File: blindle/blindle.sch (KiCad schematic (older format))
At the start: 8 parts, among them J1 CONN_5V, J2 CONN_8V, M1 74HC595, P1 pololua4988, P2 pololua4988

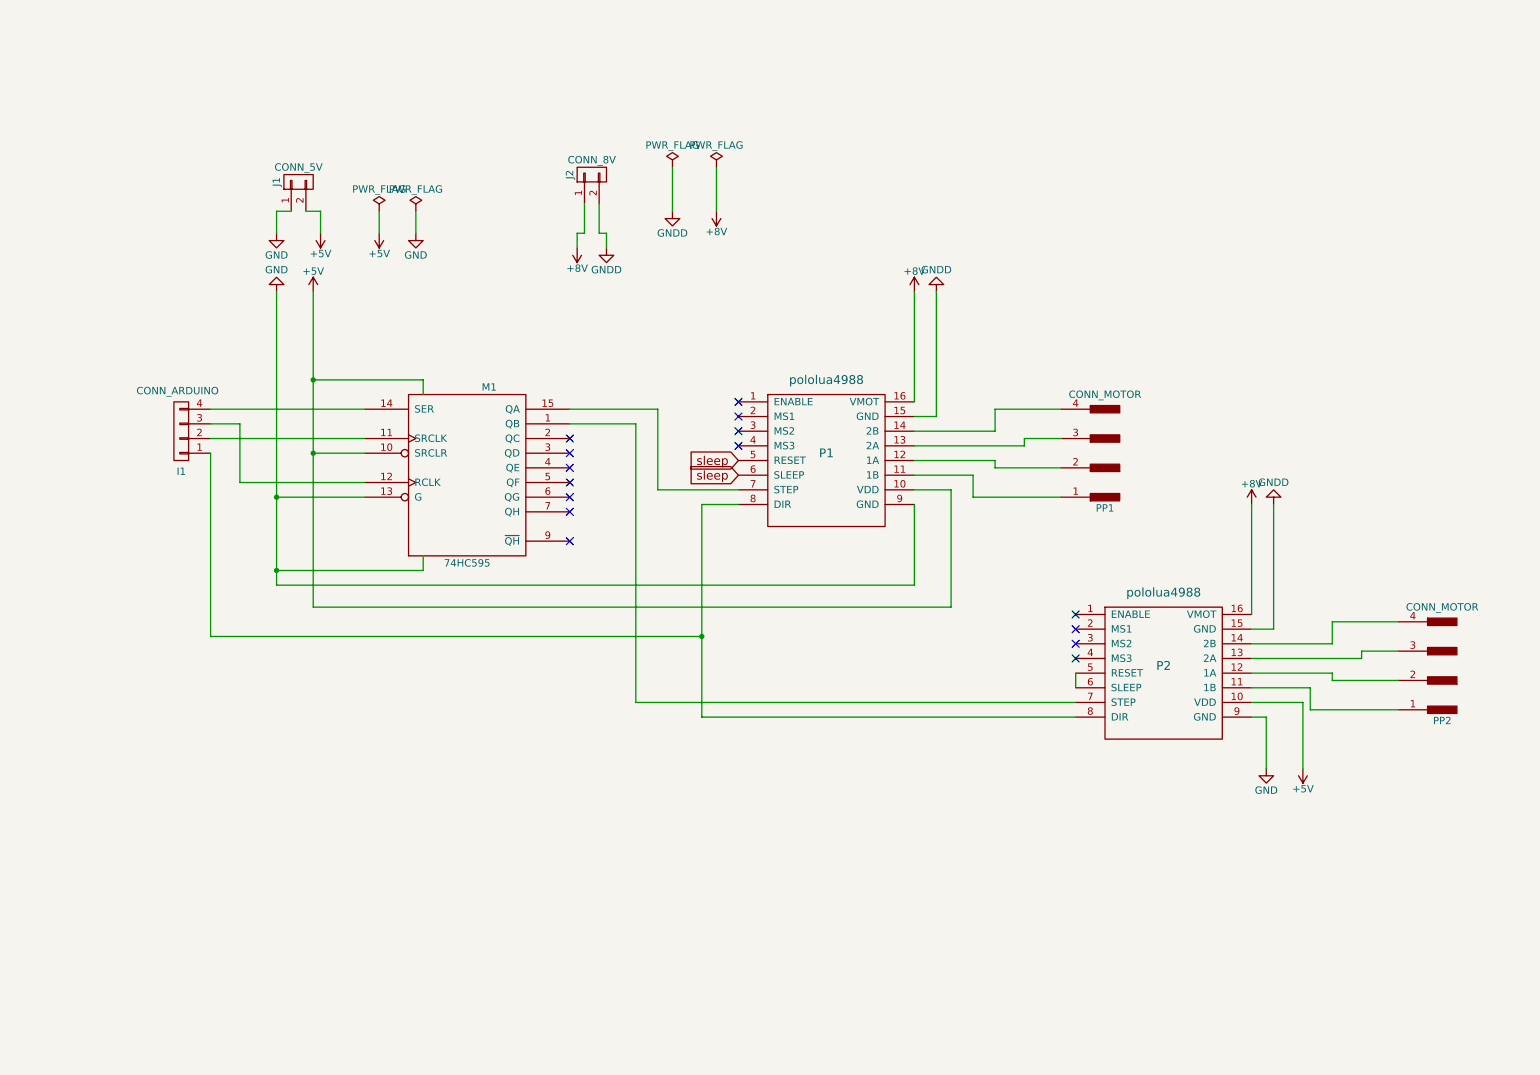
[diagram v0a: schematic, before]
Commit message: Bug en plantilla pololu - Version 4 pololus
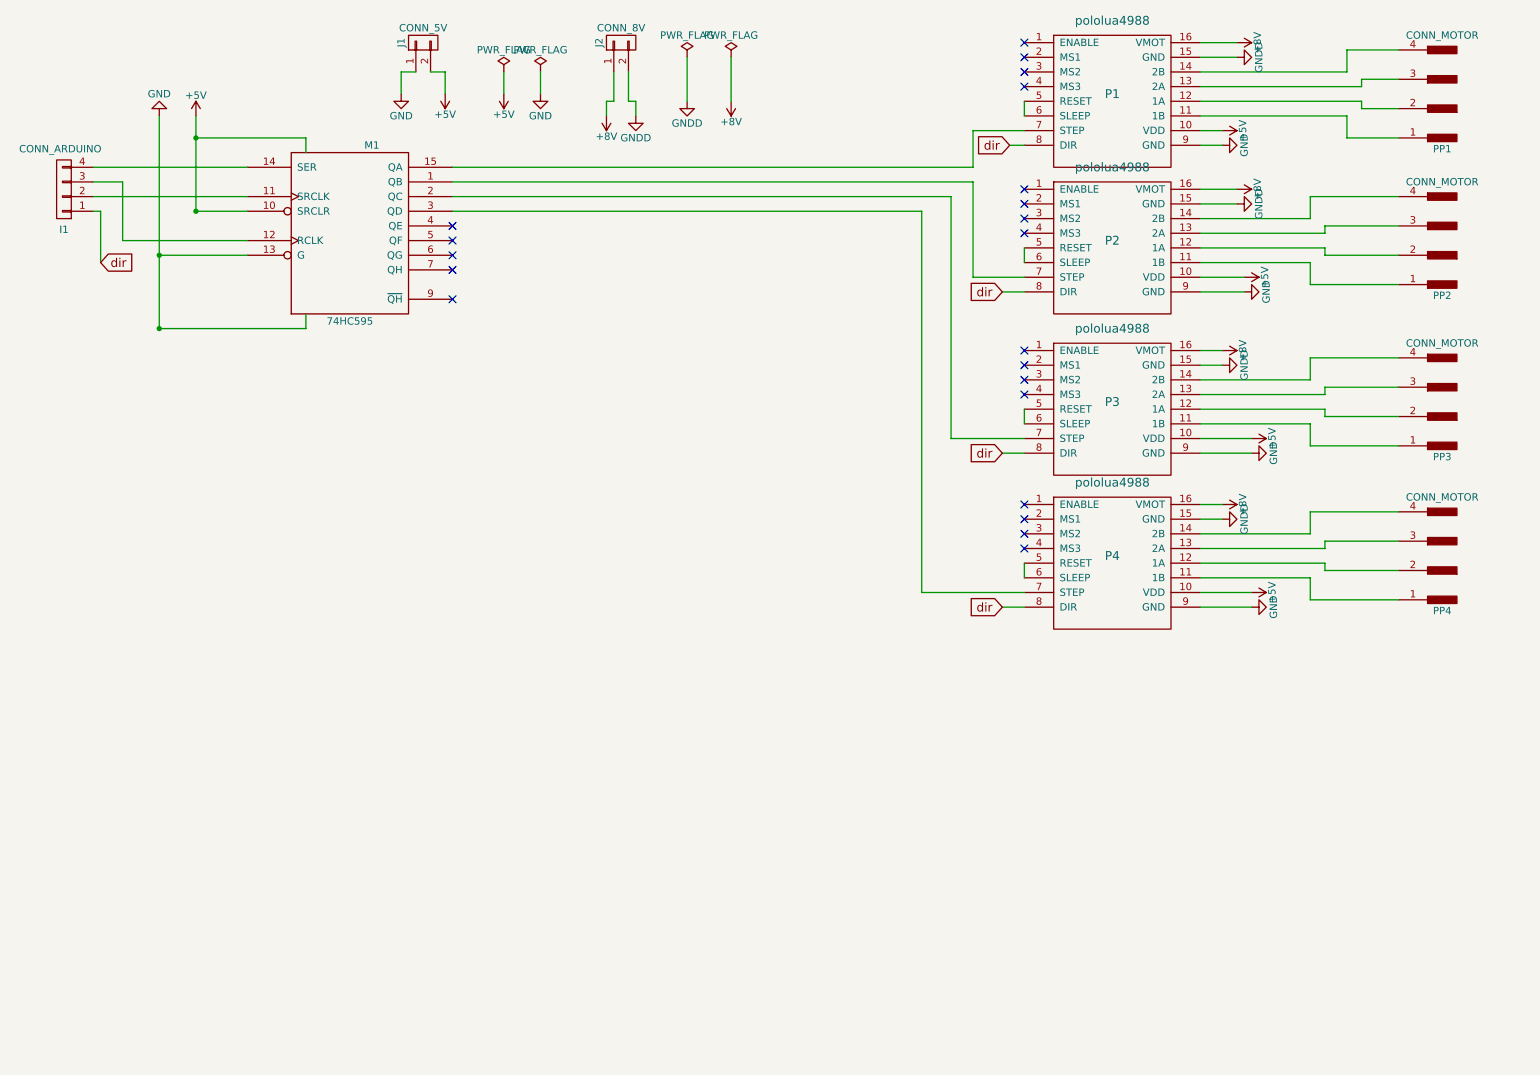
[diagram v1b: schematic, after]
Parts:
- added P3, P4: pololua4988, pololu:pololua4988, symbol pololua4988
- added PP3, PP4: CONN_MOTOR, Pin_Headers:Pin_Header_Straight_1x04_Pitch2.54mm, symbol CONN_01X04_MALE
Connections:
- net +5V: now also P3.10 (VDD), P4.10 (VDD)
- net +8V: now also P3.16 (VMOT), P4.16 (VMOT)
- net GND: now also P3.9 (GND), P4.9 (GND)
- net GNDD: now also P3.15 (GND), P4.15 (GND)
- net dir: now reaches I1.1 (P1), P1.8 (DIR), P2.8 (DIR)
- net dir: now also P3.8 (DIR), P4.8 (DIR)
- net at M1.2 (QC): now also P3.7 (STEP)
- net at M1.3 (QD): now also P4.7 (STEP)
- net sleep: no longer names the net of P1.5 (RESET), P1.6 (SLEEP)
- new net: P3.11 (1B), PP3.1
- new net: P3.12 (1A), PP3.2
- new net: P3.13 (2A), PP3.3
- new net: P3.14 (2B), PP3.4
- new net: P3.5 (RESET), P3.6 (SLEEP)
- new net: P4.11 (1B), PP4.1
- new net: P4.12 (1A), PP4.2
- new net: P4.13 (2A), PP4.3
- new net: P4.14 (2B), PP4.4
- new net: P4.5 (RESET), P4.6 (SLEEP)
- no-connect marks 15 -> 21
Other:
- moved on the sheet: I1, J1, J2, M1, P1, P2, PP1, PP2

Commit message: 8 pololu - En desarrollo
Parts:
- added I2: CONN_MULTI2, Pin_Headers:Pin_Header_Straight_1x04_Pitch2.54mm, symbol CONN_01X04
- added P5, P6, P7, P8: pololua4988, pololu:pololua4988, symbol pololua4988
- added PP5, PP6, PP7, PP8: CONN_MOTOR, Pin_Headers:Pin_Header_Straight_1x04_Pitch2.54mm, symbol CONN_01X04_MALE
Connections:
- net +5V: now also P5.10 (VDD), P6.10 (VDD), P7.10 (VDD), P8.10 (VDD)
- net +8V: now also P5.16 (VMOT), P6.16 (VMOT), P7.16 (VMOT), P8.16 (VMOT)
- net GND: now also P5.9 (GND), P6.9 (GND), P7.9 (GND), P8.9 (GND)
- net GNDD: now also P5.15 (GND), P6.15 (GND), P7.15 (GND), P8.15 (GND)
- net dir: now also P5.8 (DIR), P6.8 (DIR), P7.8 (DIR), P8.8 (DIR)
- net at I1.2 (P2), M1.11 (SRCLK): now also I2.2 (P2)
- net at I1.3 (P3), M1.12 (RCLK): now also I2.1 (P1), I2.3 (P3)
- net at M1.4 (QE): now also P5.7 (STEP)
- net at M1.5 (QF): now also P6.7 (STEP)
- net at M1.6 (QG): now also P7.7 (STEP)
- net at M1.7 (QH): now also P8.7 (STEP)
- net at M1.9 (~QH): now also I2.4 (P4)
- new net: P5.11 (1B), PP5.1
- new net: P5.12 (1A), PP5.2
- new net: P5.13 (2A), PP5.3
- new net: P5.14 (2B), PP5.4
- new net: P5.5 (RESET), P5.6 (SLEEP)
- new net: P6.11 (1B), PP6.1
- new net: P6.12 (1A), PP6.2
- new net: P6.13 (2A), PP6.3
- new net: P6.14 (2B), PP6.4
- new net: P6.5 (RESET), P6.6 (SLEEP)
- new net: P7.11 (1B), PP7.1
- new net: P7.12 (1A), PP7.2
- new net: P7.13 (2A), PP7.3
- new net: P7.14 (2B), PP7.4
- new net: P7.5 (RESET), P7.6 (SLEEP)
- new net: P8.11 (1B), PP8.1
- new net: P8.12 (1A), PP8.2
- new net: P8.13 (2A), PP8.3
- new net: P8.14 (2B), PP8.4
- new net: P8.5 (RESET), P8.6 (SLEEP)
- no-connect marks 21 -> 32

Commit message: pololu 8 - final v1 pcb
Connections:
- net dir: now also I2.1 (P1)
- net at I1.3 (P3), I2.3 (P3), M1.12 (RCLK): no longer I2.1 (P1)
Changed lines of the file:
@@
 	1500 3300 1500 1750
 Connection ~ 1500 1750
-Wire Wire Line
-	1000 3400 1600 3400
-Wire Wire Line
-	1600 3400 1600 2050
 Connection ~ 1600 2050
 Wire Wire Line
@@
 Text Label 10600 7650 0    60   ~ 0
 v1
+Text GLabel 1350 3400 2    60   Input ~ 0
+dir
+Wire Wire Line
+	1000 3400 1350 3400
 $EndSCHEMATC
